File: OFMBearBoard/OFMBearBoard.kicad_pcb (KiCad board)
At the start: 2 copper layers, 50 x 65.5 mm, 15 parts, among them J1 X Motor, J2 Y Motor, J3 Z Motor, J4 LED, J5 5V, U1 ULN2003APG, U2 ULN2003APG

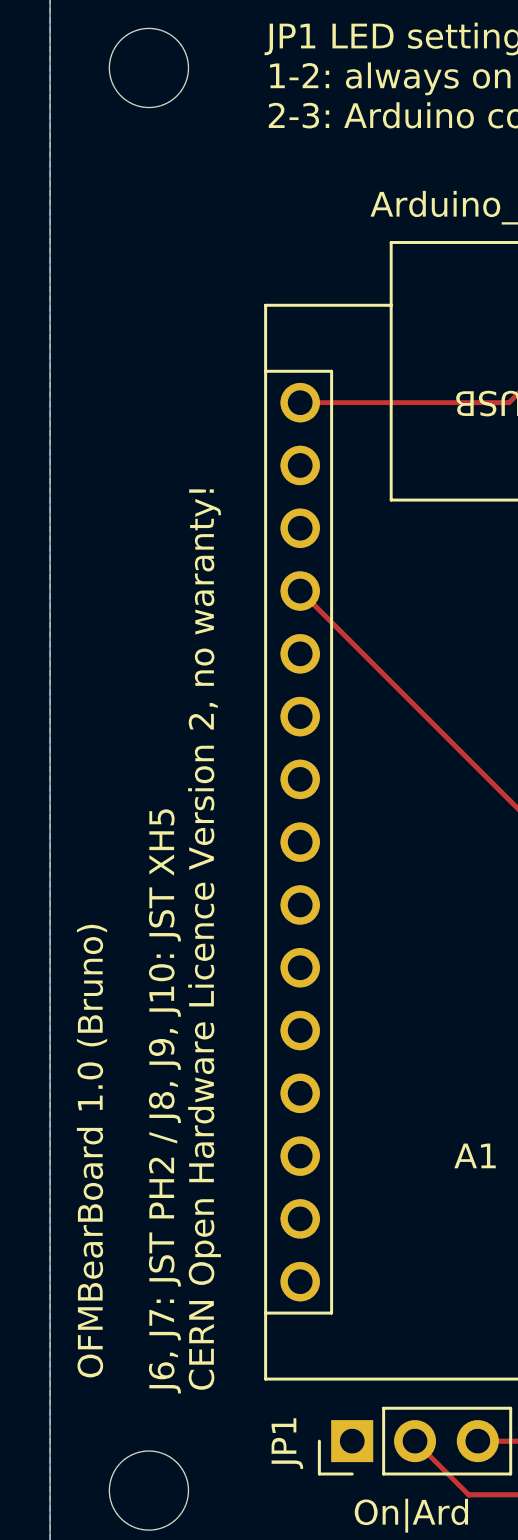
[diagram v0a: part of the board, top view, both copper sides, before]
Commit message: FIxed  https://github.com/spuelm/OFMBearBoard/issues/2
FIxed
https://github.com/spuelm/OFMBearBoard/issues/2
no functional impact: Typo Warranty with only one r
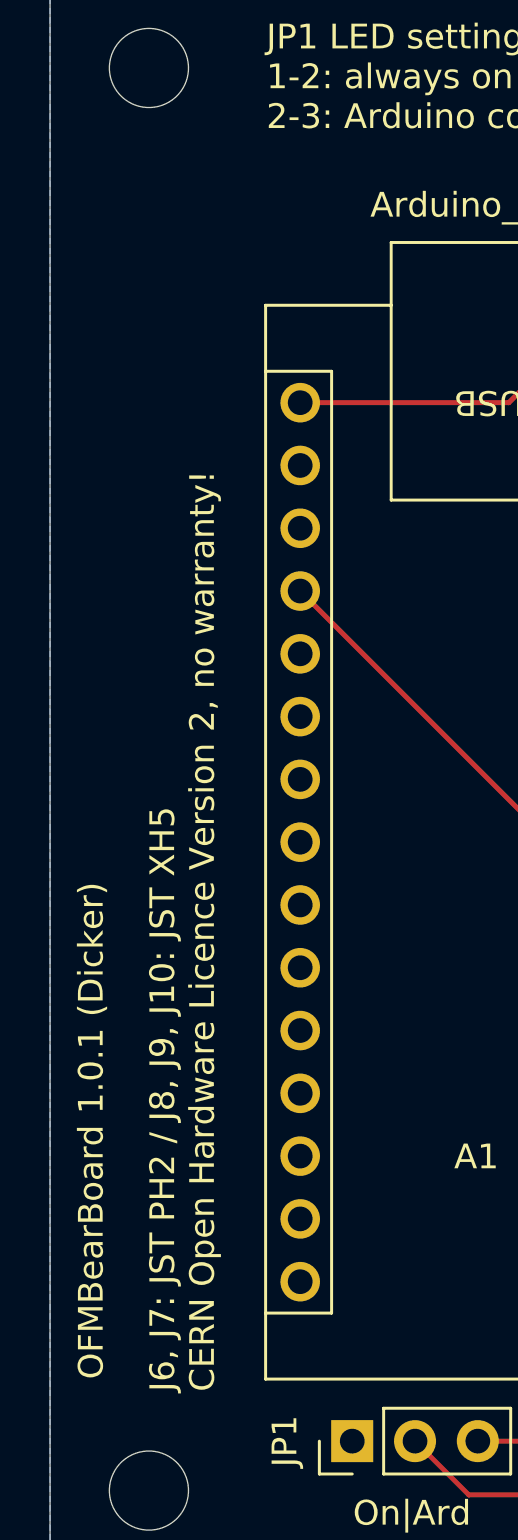
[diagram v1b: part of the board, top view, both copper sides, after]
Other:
- board text added: "J6, J7: JST PH2 / J8, J9, J10: JST XH5 ﻿CERN Open Hardware Licence Version 2, no warranty!"
- board text added: "OFMBearBoard 1.0.1 (Dicker)"
- board text removed: "J6, J7: JST PH2 / J8, J9, J10: JST XH5 ﻿CERN Open Hardware Licence Version 2, no waranty!"
- board text removed: "OFMBearBoard 1.0 (Bruno)"
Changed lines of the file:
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@@
 		(title "OFMSimpleBoard")
 		(date "2024-06-02")
-		(rev "1.1")
+		(rev "1.0.1 (Dicker)")
 	)
 	(layers
@@
 		)
 	)
-	(gr_text "OFMBearBoard 1.0 (Bruno)"
+	(gr_text "OFMBearBoard 1.0.1 (Dicker)"
 		(at 81.5 78.5 90)
 		(layer "F.SilkS")
@@
 		)
 	)
-	(gr_text "J6, J7: JST PH2 / J8, J9, J10: JST XH5\n﻿CERN Open Hardware Licence Version 2, no waranty!"
+	(gr_text "J6, J7: JST PH2 / J8, J9, J10: JST XH5\n﻿CERN Open Hardware Licence Version 2, no warranty!"
 		(at 86 79 90)
 		(layer "F.SilkS")

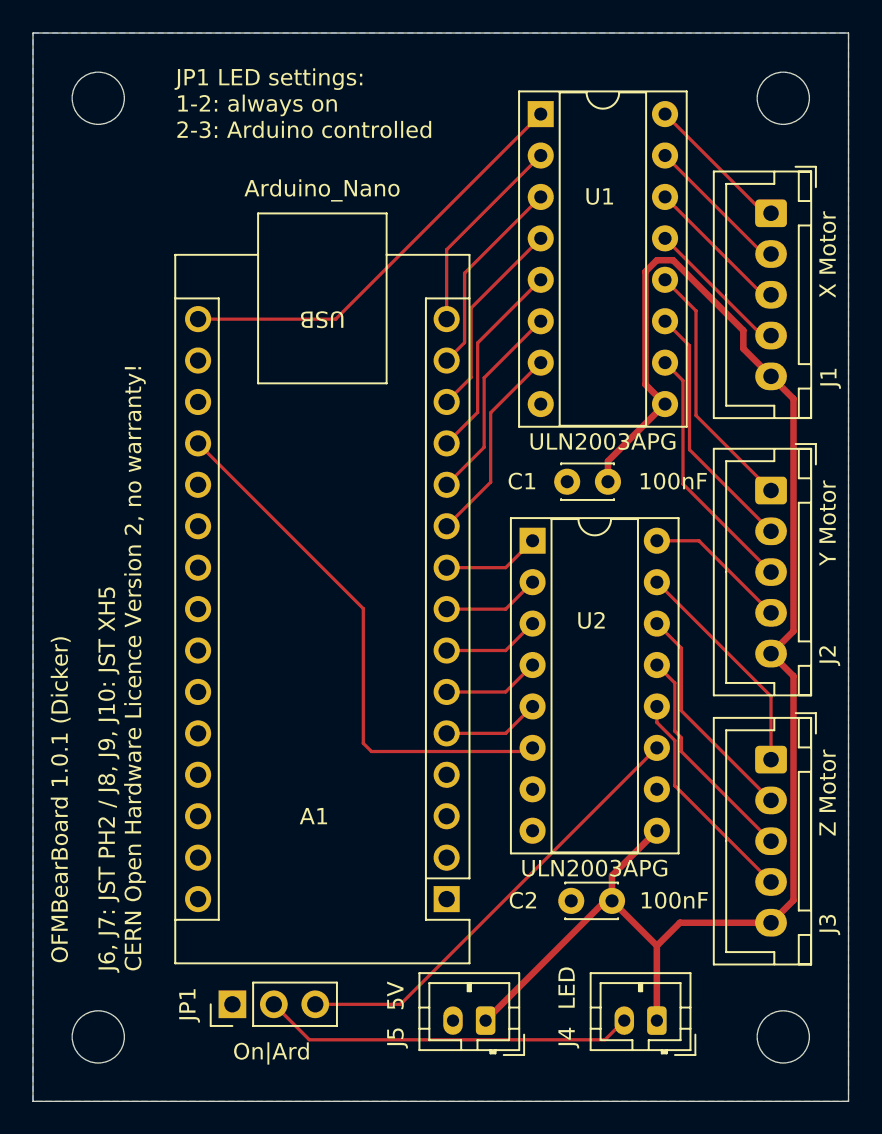
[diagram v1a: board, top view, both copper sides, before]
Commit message: Fixed IC aligment and capacitor size
Fixed IC aligment and capacitor size
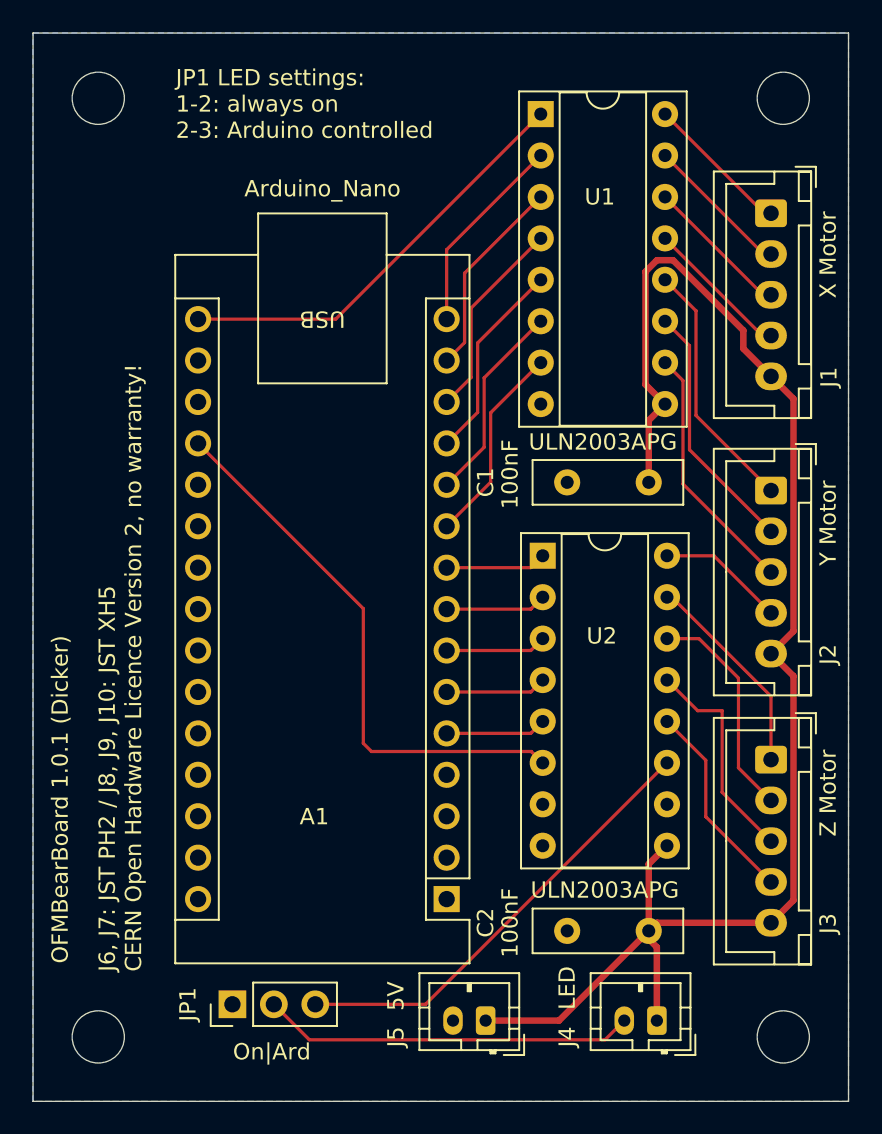
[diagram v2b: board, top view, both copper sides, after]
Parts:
- C1, C2: footprint Capacitor_THT:C_Disc_D3.0mm_W2.0mm_P2.50mm -> Capacitor_THT:C_Disc_D9.0mm_W2.5mm_P5.00mm
- moved C2 1.86 mm to (112.0, 76.5)
- moved U2 1.11 mm to (110.5, 53.5)
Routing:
- net +5V: track 94.5 -> 92.6 mm
- net /YM4: track 8.83 -> 7.83 mm
- net /ZM1: track 13.8 -> 12.8 mm
- net /A00: track 33.3 -> 34.1 mm
- net /ZM4: track 13.7 -> 13.1 mm

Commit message: New Gerber Zip
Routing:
- net +5V: track 92.6 -> 128.5 mm
- net /A00: track 34.1 -> 51.7 mm
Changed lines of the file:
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@@
-	)
-	(segment
-		(start 109.8 65.5)
-		(end 100 65.5)
-		(width 0.2)
-		(layer "F.Cu")
-		(net 16)
-	)
-	(segment
-		(start 100 65.5)
-		(end 99.5 65)
-		(width 0.2)
-		(layer "F.Cu")
-		(net 16)
 	)
 	(segment
 		(start 99.5 56.74)
-		(end 89.37 46.61)
-		(width 0.2)
-		(layer "F.Cu")
-		(net 16)
-	)
-	(segment
-		(start 99.5 65)
+		(end 99.5 73.5)
+		(width 0.2)
+		(layer "F.Cu")
+		(net 16)
+	)
+	(segment
+		(start 99.5 73.5)
+		(end 103 77)
+		(width 0.2)
+		(layer "F.Cu")
+		(net 16)
+	)
+	(segment
+		(start 89.37 46.61)
 		(end 99.5 56.74)
 		(width 0.2)
@@
 	)
 	(segment
-		(start 110.5 66.2)
-		(end 109.8 65.5)
-		(width 0.2)
-		(layer "F.Cu")
-		(net 16)
-	)
-	(segment
-		(start 117.502943 35.38)
-		(end 118.497057 35.38)
-		(width 0.4)
-		(layer "F.Cu")
-		(net 18)
-	)
-	(segment
-		(start 122.8 39.682943)
-		(end 122.8 40.8)
-		(width 0.4)
-		(layer "F.Cu")
-		(net 18)
-	)
-	(segment
-		(start 122.8 40.8)
+		(start 103 77)
+		(end 106 77)
+		(width 0.2)
+		(layer "F.Cu")
+		(net 16)
+	)
+	(segment
+		(start 106.5 70.2)
+		(end 110.5 66.2)
+		(width 0.2)
+		(layer "F.Cu")
+		(net 16)
+	)
+	(segment
+		(start 106.5 76.5)
+		(end 106.5 70.2)
+		(width 0.2)
+		(layer "F.Cu")
+		(net 16)
+	)
+	(segment
+		(start 106 77)
+		(end 106.5 76.5)
+		(width 0.2)
+		(layer "F.Cu")
+		(net 16)
+	)
+	(segment
+		(start 118 44.2)
+		(end 115.3 44.2)
+		(width 0.4)
+		(layer "F.Cu")
+		(net 18)
+	)
+	(segment
+		(start 115 26.5)
+		(end 117 24.5)
+		(width 0.4)
+		(layer "F.Cu")
+		(net 18)
+	)
+	(segment
+		(start 117.5 78.5)
+		(end 117 78.5)
+		(width 0.4)
+		(layer "F.Cu")
+		(net 18)
+	)
+	(segment
+		(start 115.3 44.2)
+		(end 115 44.5)
+		(width 0.4)
+		(layer "F.Cu")
+		(net 18)
+	)
+	(segment
+		(start 126 78.5)
+		(end 120 78.5)
+		(width 0.4)
+		(layer "F.Cu")
+		(net 18)
+	)
+	(segment
+		(start 115 44.5)
+		(end 115 26.5)
+		(width 0.4)
+		(layer "F.Cu")
+		(net 18)
+	)
+	(segment
+		(start 117 24.5)
+		(end 119 24.5)
+		(width 0.4)
+		(layer "F.Cu")
+		(net 18)
+	)
+	(segment
+		(start 124.5 59.5)
+		(end 126.5 59.5)
+		(width 0.4)
+		(layer "F.Cu")
+		(net 18)
+	)
+	(segment
+		(start 124.5 76)
+		(end 126.5 76)
+		(width 0.4)
+		(layer "F.Cu")
+		(net 18)
+	)
+	(segment
+		(start 126.5 76)
+		(end 126.5 78)
+		(width 0.4)
+		(layer "F.Cu")
+		(net 18)
+	)
+	(segment
+		(start 120 73.16)
+		(end 120 78.5)
+		(width 0.4)
+		(layer "F.Cu")
+		(net 18)
+	)
+	(segment
+		(start 110.5 78.5)
+		(end 107 82)
+		(width 0.4)
+		(layer "F.Cu")
+		(net 18)
+	)
+	(segment
+		(start 117.5 82)
+		(end 117.5 78.5)
+		(width 0.4)
+		(layer "F.Cu")
+		(net 18)
+	)
+	(segment
+		(start 115 47)
+		(end 117 49)
+		(width 0.4)
+		(layer "F.Cu")
+		(net 18)
+	)
+	(segment
+		(start 126.5 42.5)
+		(end 126.5 32)
+		(width 0.4)
+		(layer "F.Cu")
+		(net 18)
+	)
+	(segment
+		(start 126.5 78)
+		(end 126 78.5)
+		(width 0.4)
+		(layer "F.Cu")
+		(net 18)
+	)
+	(segment
+		(start 118.12 71.28)
+		(end 120 73.16)
+		(width 0.4)
+		(layer "F.Cu")
+		(net 18)
+	)
+	(segment
+		(start 120 78.5)
+		(end 117.5 78.5)
+		(width 0.4)
+		(layer "F.Cu")
+		(net 18)
+	)
+	(segment
+		(start 117 76.5)
+		(end 117 78.5)
+		(width 0.4)
+		(layer "F.Cu")
+		(net 18)
+	)
+	(segment
+		(start 126.5 59.5)
+		(end 126.5 76)
+		(width 0.4)
+		(layer "F.Cu")
+		(net 18)
+	)
+	(segment
+		(start 117 78.5)
+		(end 110.5 78.5)
+		(width 0.4)
+		(layer "F.Cu")
+		(net 18)
+	)
+	(segment
+		(start 126.5 42.5)
+		(end 126.5 59.5)
+		(width 0.4)
+		(layer "F.Cu")
+		(net 18)
+	)
+	(segment
+		(start 115 44.5)
+		(end 115 47)
+		(width 0.4)
+		(layer "F.Cu")
+		(net 18)
+	)
+	(segment
+		(start 119 24.5)
+		(end 126.5 32)
+		(width 0.4)
+		(layer "F.Cu")
+		(net 18)
+	)
+	(segment
+		(start 126.5 42.5)
 		(end 124.5 42.5)
 		(width 0.4)
 		(layer "F.Cu")
-		(net 18)
-	)
-	(segment
-		(start 117 45.2)
-		(end 118 44.2)
-		(width 0.4)
-		(layer "F.Cu")
-		(net 18)
-	)
-	(segment
-		(start 117 49)
-		(end 117 45.2)
-		(width 0.4)
-		(layer "F.Cu")
-		(net 18)
-	)
-	(segment
-		(start 118 44.2)
-		(end 116.8 43)
-		(width 0.4)
-		(layer "F.Cu")
-		(net 18)
-	)
-	(segment
-		(start 117 77)
-		(end 117.5 77.5)
-		(width 0.4)
-		(layer "F.Cu")
-		(net 18)
-	)
-	(segment
-		(start 125.875 43.875)
-		(end 124.5 42.5)
-		(width 0.4)
-		(layer "F.Cu")
-		(net 18)
-	)
-	(segment
-		(start 107 82)
-		(end 111.5 82)
-		(width 0.4)
-		(layer "F.Cu")
-		(net 18)
-	)
-	(segment
-		(start 117 76.5)
-		(end 117 72.4)
-		(width 0.4)
-		(layer "F.Cu")
-		(net 18)
-	)
-	(segment
-		(start 117 76.5)
-		(end 117 77)
-		(width 0.4)
-		(layer "F.Cu")
-		(net 18)
-	)
-	(segment
-		(start 124.5 76)
-		(end 117.5 76)
-		(width 0.4)
-		(layer "F.Cu")
-		(net 18)
-	)
-	(segment
-		(start 125.875 60.875)
-		(end 124.5 59.5)
-		(width 0.4)
-		(layer "F.Cu")
-		(net 18)
-	)
-	(segment
-		(start 125.875 58.125)
-		(end 125.875 43.875)
-		(width 0.4)
-		(layer "F.Cu")
-		(net 18)
-	)
-	(segment
-		(start 117.5 76)
-		(end 117 76.5)
-		(width 0.4)
-		(layer "F.Cu")
-		(net 18)
-	)
-	(segment
-		(start 124.5 76)
-		(end 125.875 74.625)
-		(width 0.4)
-		(layer "F.Cu")
-		(net 18)
-	)
-	(segment
-		(start 116.8 36.082943)
-		(end 117.502943 35.38)
-		(width 0.4)
-		(layer "F.Cu")
-		(net 18)
-	)
-	(segment
-		(start 117 72.4)
-		(end 118.12 71.28)
-		(width 0.4)
-		(layer "F.Cu")
-		(net 18)
-	)
-	(segment
-		(start 118.497057 35.38)
-		(end 122.8 39.682943)
-		(width 0.4)
-		(layer "F.Cu")
-		(net 18)
-	)
-	(segment
-		(start 124.5 59.5)
-		(end 125.875 58.125)
-		(width 0.4)
-		(layer "F.Cu")
-		(net 18)
-	)
-	(segment
-		(start 117.5 77.5)
-		(end 117.5 82)
-		(width 0.4)
-		(layer "F.Cu")
-		(net 18)
-	)
-	(segment
-		(start 125.875 74.625)
-		(end 125.875 60.875)
-		(width 0.4)
-		(layer "F.Cu")
-		(net 18)
-	)
-	(segment
-		(start 116.8 43)
-		(end 116.8 36.082943)
-		(width 0.4)
-		(layer "F.Cu")
-		(net 18)
-	)
-	(segment
-		(start 111.5 82)
-		(end 117 76.5)
-		(width 0.4)
-		(layer "F.Cu")
